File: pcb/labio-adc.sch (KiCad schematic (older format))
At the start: 10 parts

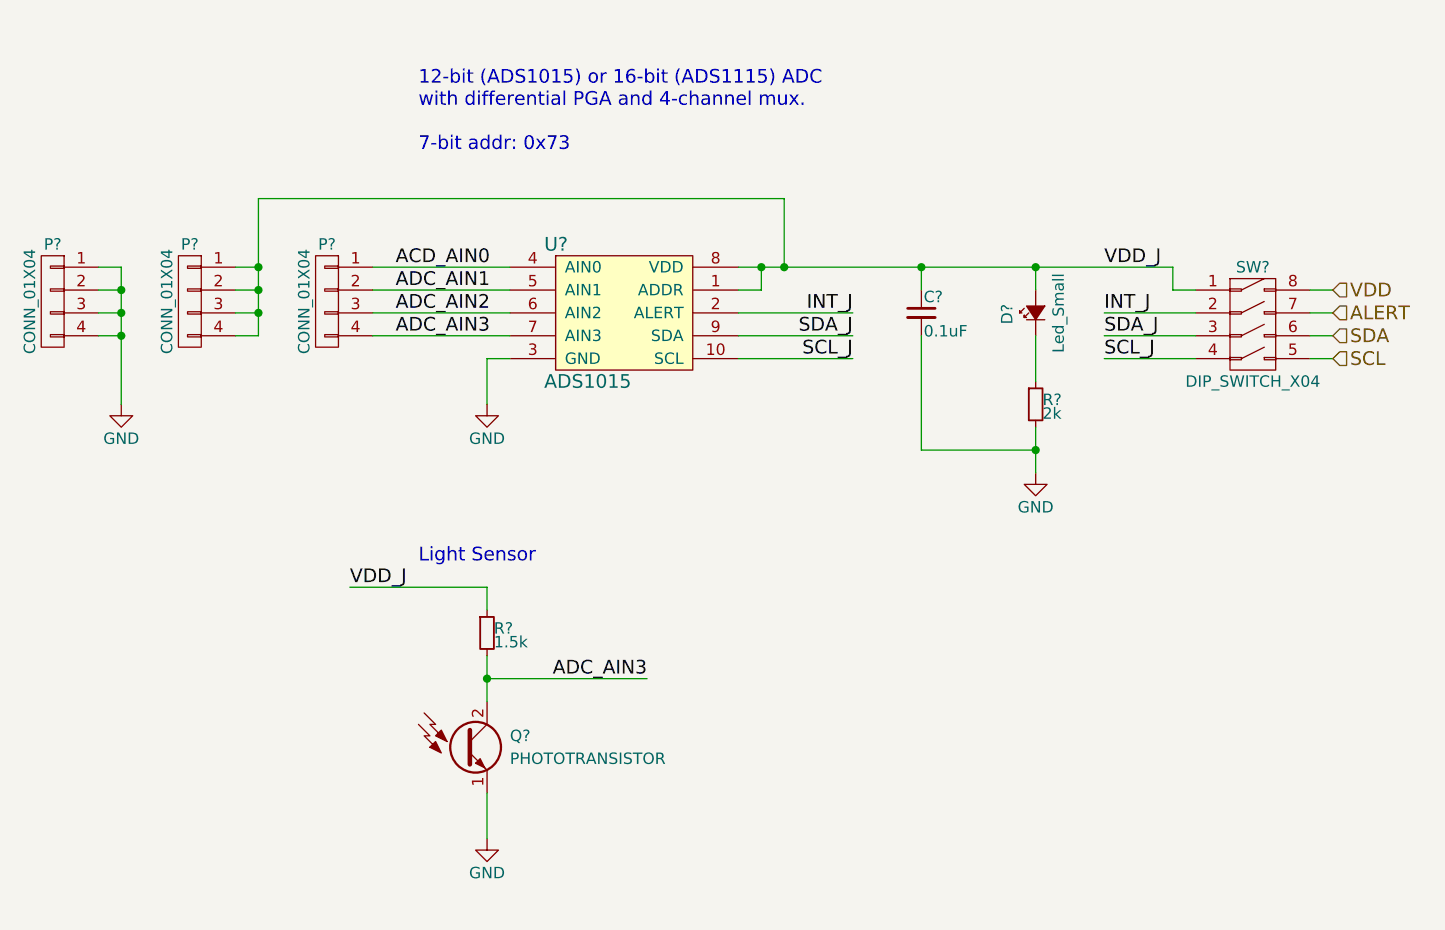
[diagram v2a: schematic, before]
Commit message: make extra footprints. start floorplan. fix display nets. add power expansion header.
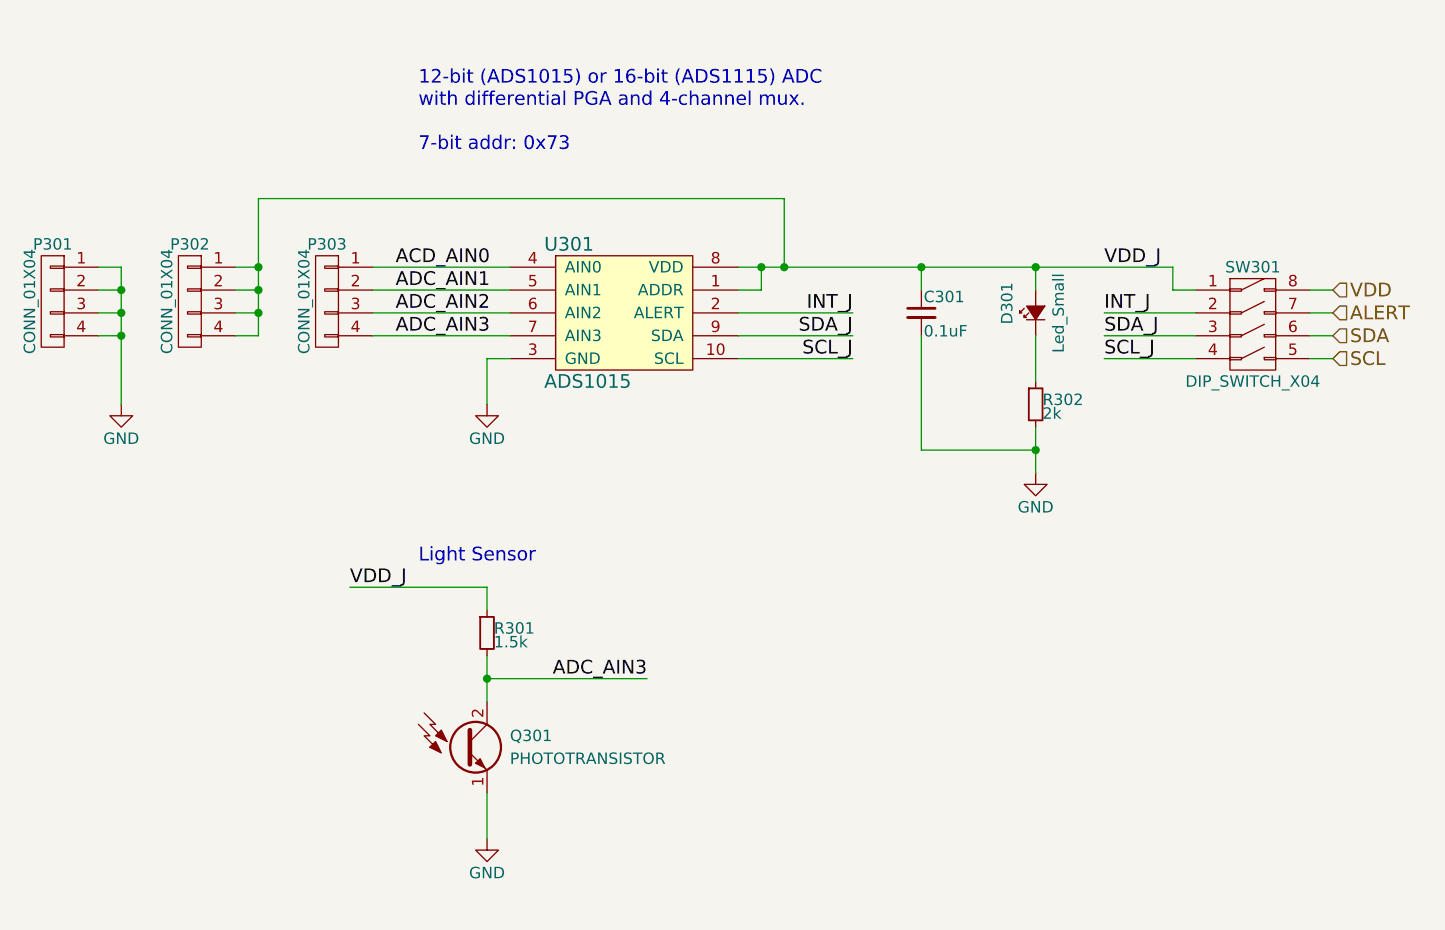
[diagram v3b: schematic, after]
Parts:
- C301: renamed from C?; footprint (none) -> Capacitors_SMD:C_0603
- D301: renamed from D?; footprint (none) -> LEDs:LED-0603
- P301, P302, P303: renamed from P?; footprint (none) -> Pin_Headers:Pin_Header_Straight_1x04
- Q301: renamed from Q?; footprint (none) -> LEDs:LED-0603
- R301, R302: renamed from R?; footprint (none) -> Resistors_SMD:R_0603
- SW301: renamed from SW?; footprint (none) -> labio-special:DIP-8_W7.62mm_SMT
- U301: renamed from U?; footprint (none) -> Housings_SSOP:MSOP-10_3x3mm_Pitch0.5mm
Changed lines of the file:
@@
 $Descr A4 11693 8268
 encoding utf-8
-Sheet 3 8
+Sheet 3 9
 Title ""
 Date ""
@@
 $EndDescr
 $Comp
-L ADS1015 U?
+L ADS1015 U301
 U 1 1 574C563E
 P 6300 3400
-F 0 "U?" H 5950 3700 60  0000 L CNN
+F 0 "U301" H 5950 3700 60  0000 L CNN
 F 1 "ADS1015" H 5950 3100 60  0000 L CNN
-F 2 "" H 6300 3400 60  0000 C CNN
+F 2 "Housings_SSOP:MSOP-10_3x3mm_Pitch0.5mm" H 6300 3400 60  0001 C CNN
 F 3 "" H 6300 3400 60  0000 C CNN
 	1    6300 3400
@@
 $EndComp
 $Comp
-L CONN_01X04 P?
+L CONN_01X04 P301
 U 1 1 574C66B3
 P 3800 3350
-F 0 "P?" H 3800 3600 50  0000 C CNN
+F 0 "P301" H 3800 3600 50  0000 C CNN
 F 1 "CONN_01X04" V 3900 3350 50  0000 C CNN
-F 2 "" H 3800 3350 50  0000 C CNN
+F 2 "Pin_Headers:Pin_Header_Straight_1x04" H 3800 3350 50  0001 C CNN
 F 3 "" H 3800 3350 50  0000 C CNN
 	1    3800 3350
@@
 $EndComp
 $Comp
-L CONN_01X04 P?
+L CONN_01X04 P302
 U 1 1 574C66E4
 P 4400 3350
-F 0 "P?" H 4400 3600 50  0000 C CNN
+F 0 "P302" H 4400 3600 50  0000 C CNN
 F 1 "CONN_01X04" V 4500 3350 50  0000 C CNN
-F 2 "" H 4400 3350 50  0000 C CNN
+F 2 "Pin_Headers:Pin_Header_Straight_1x04" H 4400 3350 50  0001 C CNN
 F 3 "" H 4400 3350 50  0000 C CNN
 	1    4400 3350
@@
 $EndComp
 $Comp
-L CONN_01X04 P?
+L CONN_01X04 P303
 U 1 1 574C66FC
 P 5000 3350
-F 0 "P?" H 5000 3600 50  0000 C CNN
+F 0 "P303" H 5000 3600 50  0000 C CNN
 F 1 "CONN_01X04" V 5100 3350 50  0000 C CNN
-F 2 "" H 5000 3350 50  0000 C CNN
+F 2 "Pin_Headers:Pin_Header_Straight_1x04" H 5000 3350 50  0001 C CNN
 F 3 "" H 5000 3350 50  0000 C CNN
 	1    5000 3350
@@
 $EndComp
 $Comp
-L GND #PWR?
+L GND #PWR05
 U 1 1 574C6823
 P 5700 3800
-F 0 "#PWR?" H 5700 3550 50  0001 C CNN
+F 0 "#PWR05" H 5700 3550 50  0001 C CNN
 F 1 "GND" H 5700 3650 50  0000 C CNN
 F 2 "" H 5700 3800 50  0000 C CNN
@@
 $EndComp
 $Comp
-L C_Small C?
+L C_Small C301
 U 1 1 574C68FF
 P 7600 3400
-F 0 "C?" H 7610 3470 50  0000 L CNN
+F 0 "C301" H 7610 3470 50  0000 L CNN
 F 1 "0.1uF" H 7610 3320 50  0000 L CNN
-F 2 "" H 7600 3400 50  0000 C CNN
+F 2 "Capacitors_SMD:C_0603" H 7600 3400 50  0001 C CNN
 F 3 "" H 7600 3400 50  0000 C CNN
 	1    7600 3400
@@
 	5700 3600 5800 3600
 Wire Wire Line
-	4100 3200 4100 3300
-Wire Wire Line
-	4100 3300 4100 3400
-Wire Wire Line
-	4100 3400 4100 3500
-Wire Wire Line
-	4100 3500 4100 3800
+	4100 3200 4100 3800
 Wire Wire Line
 	4100 3200 4000 3200
@@
 	4700 3500 4600 3500
 Wire Wire Line
-	4700 2900 4700 3200
-Wire Wire Line
-	4700 3200 4700 3300
-Wire Wire Line
-	4700 3300 4700 3400
-Wire Wire Line
-	4700 3400 4700 3500
+	4700 2900 4700 3500
 Wire Wire Line
 	4700 2900 7000 2900
@@
 	5200 3500 5800 3500
 $Comp
-L PHOTOTRANSISTOR Q?
+L PHOTOTRANSISTOR Q301
 U 1 1 576D542D
 P 5600 5300
-F 0 "Q?" H 5800 5350 50  0000 L CNN
+F 0 "Q301" H 5800 5350 50  0000 L CNN
 F 1 "PHOTOTRANSISTOR" H 5800 5250 50  0000 L CNN
-F 2 "" H 5800 5400 50  0000 C CNN
+F 2 "LEDs:LED-0603" H 5800 5400 50  0001 C CNN
 F 3 "" H 5600 5300 50  0000 C CNN
 	1    5600 5300
@@
 $EndComp
 $Comp
-L GND #PWR?
+L GND #PWR06
 U 1 1 576D549A
 P 5700 5700
-F 0 "#PWR?" H 5700 5450 50  0001 C CNN
+F 0 "#PWR06" H 5700 5450 50  0001 C CNN
 F 1 "GND" H 5700 5550 50  0000 C CNN
 F 2 "" H 5700 5700 50  0000 C CNN
@@
 $EndComp
 $Comp
-L R_Small R?
+L R_Small R301
 U 1 1 576D54B9
 P 5700 4800
-F 0 "R?" H 5730 4820 50  0000 L CNN
+F 0 "R301" H 5730 4820 50  0000 L CNN
 F 1 "1.5k" H 5730 4760 50  0000 L CNN
-F 2 "" H 5700 4800 50  0000 C CNN
+F 2 "Resistors_SMD:R_0603" H 5700 4800 50  0001 C CNN
 F 3 "" H 5700 4800 50  0000 C CNN
 	1    5700 4800
@@
 	5700 4600 5100 4600
 Wire Wire Line
-	5700 4900 5700 5000
-Wire Wire Line
-	5700 5000 5700 5100
+	5700 4900 5700 5100
 Wire Wire Line
 	5700 5000 6400 5000
@@
 ADC_AIN3
 $Comp
-L DIP_SWITCH_X04 SW?
+L DIP_SWITCH_X04 SW301
 U 1 1 576D562D
 P 9050 3450
-F 0 "SW?" H 9050 3700 50  0000 C CNN
+F 0 "SW301" H 9050 3700 50  0000 C CNN
 F 1 "DIP_SWITCH_X04" H 9050 3200 50  0000 C CNN
-F 2 "" H 9050 2250 50  0000 C CNN
+F 2 "labio-special:DIP-8_W7.62mm_SMT" H 9050 2250 50  0001 C CNN
 F 3 "" H 9050 2250 50  0000 C CNN
 	1    9050 3450
@@
 $EndComp
 $Comp
-L Led_Small D?
+L Led_Small D301
 U 1 1 576D57C2
 P 8100 3400
-F 0 "D?" H 8050 3525 50  0000 L CNN
+F 0 "D301" H 8050 3525 50  0000 L CNN
 F 1 "Led_Small" H 7925 3300 50  0000 L CNN
-F 2 "" V 8100 3400 50  0000 C CNN
+F 2 "LEDs:LED-0603" V 8100 3400 50  0001 C CNN
 F 3 "" V 8100 3400 50  0000 C CNN
 	1    8100 3400
@@
 $EndComp
 $Comp
-L R_Small R?
+L R_Small R302
 U 1 1 576D5877
 P 8100 3800
-F 0 "R?" H 8130 3820 50  0000 L CNN
+F 0 "R302" H 8130 3820 50  0000 L CNN
 F 1 "2k" H 8130 3760 50  0000 L CNN
-F 2 "" H 8100 3800 50  0000 C CNN
+F 2 "Resistors_SMD:R_0603" H 8100 3800 50  0001 C CNN
 F 3 "" H 8100 3800 50  0000 C CNN
 	1    8100 3800
@@
 	5700 3800 5700 3600
 $Comp
-L GND #PWR?
+L GND #PWR07
 U 1 1 576D595B
 P 4100 3800
-F 0 "#PWR?" H 4100 3550 50  0001 C CNN
+F 0 "#PWR07" H 4100 3550 50  0001 C CNN
 F 1 "GND" H 4100 3650 50  0000 C CNN
 F 2 "" H 4100 3800 50  0000 C CNN
@@
 $EndComp
 $Comp
-L GND #PWR?
+L GND #PWR08
 U 1 1 576D5995
 P 8100 4100
-F 0 "#PWR?" H 8100 3850 50  0001 C CNN
+F 0 "#PWR08" H 8100 3850 50  0001 C CNN
 F 1 "GND" H 8100 3950 50  0000 C CNN
 F 2 "" H 8100 4100 50  0000 C CNN
@@
 $EndComp
 Wire Wire Line
-	8100 3900 8100 4000
-Wire Wire Line
-	8100 4000 8100 4100
+	8100 3900 8100 4100
 Wire Wire Line
 	8100 4000 7600 4000
@@
 	8700 3300 8700 3200
 Wire Wire Line
-	8700 3200 8100 3200
-Wire Wire Line
-	8100 3200 7600 3200
-Wire Wire Line
-	7600 3200 7000 3200
-Wire Wire Line
-	7000 3200 6900 3200
-Wire Wire Line
-	6900 3200 6800 3200
+	8700 3200 6800 3200
 Wire Wire Line
 	6900 3300 6900 3200

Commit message: update imu parts, adc rails, motor headers
* replace LSM303C accelerometer with LSM303D for better sensor ranges at same cost.
* add L3GD20H gyroscope so we have a 10-DOF imu. consider leaving depopulated for complexity.
* add 0 ohms to accel/gyro address and interrupt pins in case of later changes
* change ADC rails to 5V to read 5V power shunts. add level shifters to the 3.3V I2C bus.
* use 3.5mm pitch headers for motor terminal blocks to accept higher guage wire.

todo:
* redo ADC routing
* make space behind motor headers
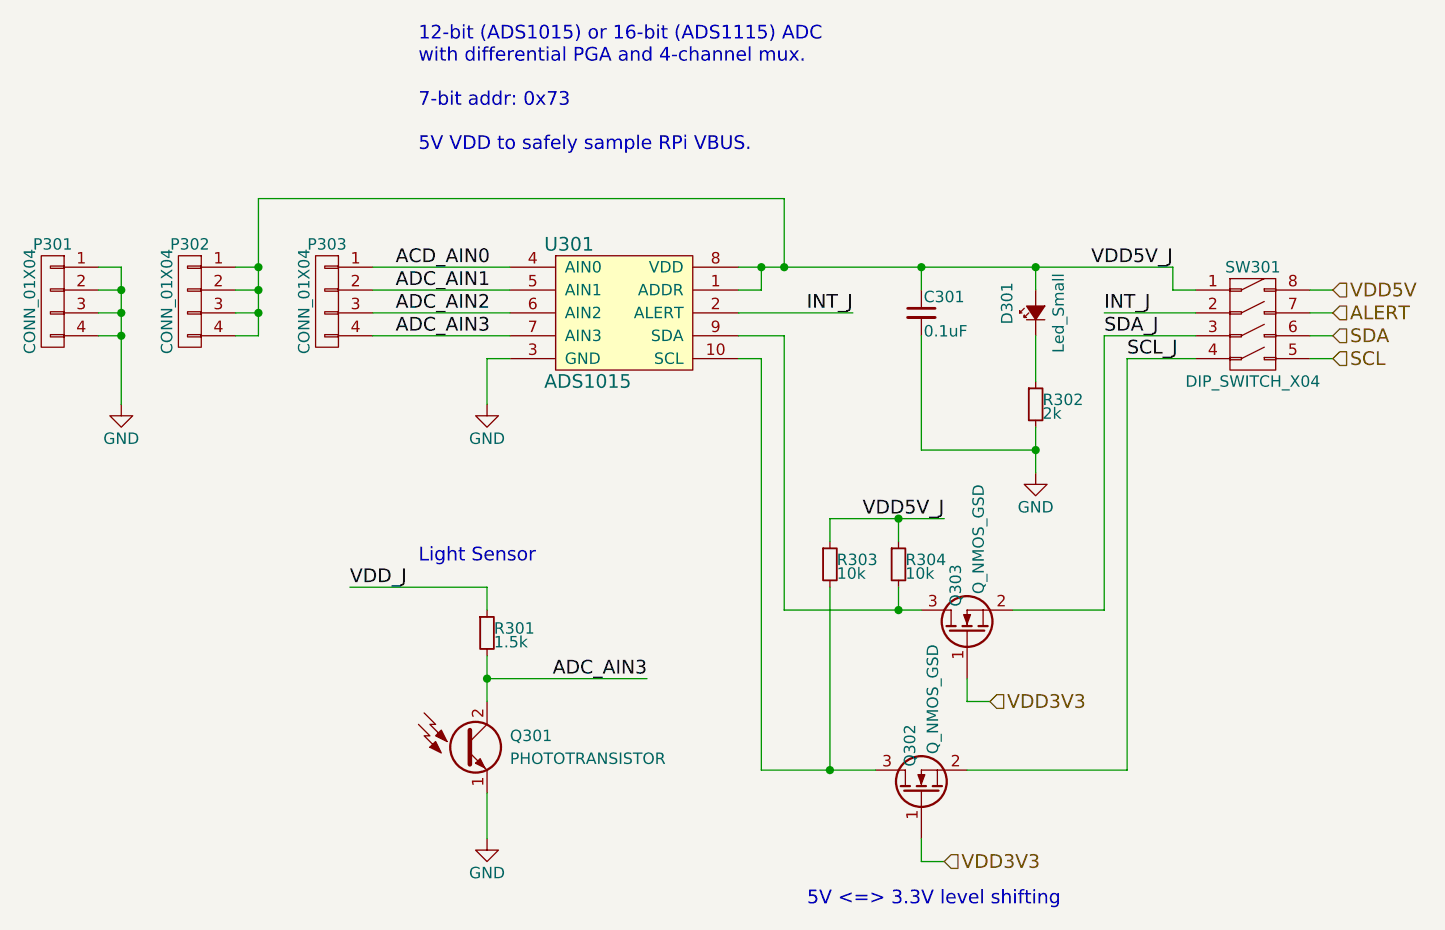
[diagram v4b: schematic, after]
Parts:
- added Q302, Q303: Q_NMOS_GSD, TO_SOT_Packages_SMD:SOT-23, symbol Q_NMOS_GSD
- added R303, R304: 10k, Resistors_SMD:R_0603, symbol R_Small
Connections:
- net SCL_J: now also Q302.2 (S); no longer U301.10 (SCL)
- net SDA_J: now also Q303.2 (S); no longer U301.9 (SDA)
- net VDD_J: no longer C301.1, D301.2 (A), P302.1 (P1), P302.2 (P2), P302.3 (P3), P302.4 (P4), SW301.1 (1A), U301.1 (ADDR), U301.8 (VDD)
- net VDD renamed VDD5V
- new net: Q302.3 (D), R303.2, U301.10 (SCL)
- new net: Q303.3 (D), R304.2, U301.9 (SDA)
- new net VDD3V3: Q302.1 (G), Q303.1 (G)
- new net VDD5V_J: C301.1, D301.2 (A), P302.1 (P1), P302.2 (P2), P302.3 (P3), P302.4 (P4), R303.1, R304.1, SW301.1 (1A), U301.1 (ADDR), U301.8 (VDD)
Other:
- note added: "12-bit (ADS1015) or 16-bit (ADS1115) ADC\nwith differential PGA and 4-channel mux.\n\n7-bit addr: 0x73\n\n5V VDD to safely sample RPi VBUS."
- note added: "5V <=> 3.3V level shifting"
- note removed: "12-bit (ADS1015) or 16-bit (ADS1115) ADC\nwith differential PGA and 4-channel mux.\n\n7-bit addr: 0x73"
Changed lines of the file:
@@
 $EndComp
 Text HLabel 9400 3300 2    60   Input ~ 0
-VDD
+VDD5V
 Text HLabel 9400 3500 2    60   Input ~ 0
 SDA
@@
 	6800 3400 7300 3400
 Wire Wire Line
-	7300 3500 6800 3500
-Wire Wire Line
-	6800 3600 7300 3600
-Wire Wire Line
 	5200 3200 5800 3200
 Wire Wire Line
@@
 	6800 3300 6900 3300
 Text Notes 5400 2700 0    60   ~ 0
-12-bit (ADS1015) or 16-bit (ADS1115) ADC\nwith differential PGA and 4-channel mux.\n\n7-bit addr: 0x73
+12-bit (ADS1015) or 16-bit (ADS1115) ADC\nwith differential PGA and 4-channel mux.\n\n7-bit addr: 0x73\n\n5V VDD to safely sample RPi VBUS.
 Text Label 5300 3200 0    60   ~ 0
 ACD_AIN0
@@
 	8400 3500 8800 3500
 Wire Wire Line
-	8800 3600 8400 3600
+	8800 3600 8500 3600
 Wire Wire Line
 	8800 3300 8700 3300
@@
 Wire Wire Line
 	9300 3600 9400 3600
-Text Label 8400 3200 0    60   ~ 0
-VDD_J
+Text Label 8700 3200 2    60   ~ 0
+VDD5V_J
 Text Label 8400 3400 0    60   ~ 0
 INT_J
 Text Label 8400 3500 0    60   ~ 0
 SDA_J
-Text Label 8400 3600 0    60   ~ 0
+Text Label 8500 3600 0    60   ~ 0
 SCL_J
 Text Label 7300 3400 2    60   ~ 0
 INT_J
-Text Label 7300 3500 2    60   ~ 0
-SDA_J
-Text Label 7300 3600 2    60   ~ 0
-SCL_J
 Text Label 5100 4600 0    60   ~ 0
 VDD_J
+$Comp
+L Q_NMOS_GSD Q303
+U 1 1 578AEC2F
+P 7800 4800
+F 0 "Q303" H 8100 4850 50  0000 R CNN
+F 1 "Q_NMOS_GSD" H 8450 4750 50  0000 R CNN
+F 2 "TO_SOT_Packages_SMD:SOT-23" H 8000 4900 50  0001 C CNN
+F 3 "" H 7800 4800 50  0000 C CNN
+	1    7800 4800
+	0    -1   -1   0
+$EndComp
+$Comp
+L Q_NMOS_GSD Q302
+U 1 1 578AECE5
+P 7600 5500
+F 0 "Q302" H 7900 5550 50  0000 R CNN
+F 1 "Q_NMOS_GSD" H 8250 5450 50  0000 R CNN
+F 2 "TO_SOT_Packages_SMD:SOT-23" H 7800 5600 50  0001 C CNN
+F 3 "" H 7600 5500 50  0000 C CNN
+	1    7600 5500
+	0    -1   -1   0
+$EndComp
+$Comp
+L R_Small R304
+U 1 1 578AED3B
+P 7500 4500
+F 0 "R304" H 7530 4520 50  0000 L CNN
+F 1 "10k" H 7530 4460 50  0000 L CNN
+F 2 "Resistors_SMD:R_0603" H 7500 4500 50  0001 C CNN
+F 3 "" H 7500 4500 50  0000 C CNN
+	1    7500 4500
+	1    0    0    -1
+$EndComp
+$Comp
+L R_Small R303
+U 1 1 578AED89
+P 7200 4500
+F 0 "R303" H 7230 4520 50  0000 L CNN
+F 1 "10k" H 7230 4460 50  0000 L CNN
+F 2 "Resistors_SMD:R_0603" H 7200 4500 50  0001 C CNN
+F 3 "" H 7200 4500 50  0000 C CNN
+	1    7200 4500
+	1    0    0    -1
+$EndComp
+Wire Wire Line
+	7800 5000 7800 5100
+Wire Wire Line
+	7800 5100 7900 5100
+Wire Wire Line
+	7600 5700 7600 5800
+Wire Wire Line
+	7600 5800 7700 5800
+Text HLabel 7900 5100 2    60   Input ~ 0
+VDD3V3
+Text HLabel 7700 5800 2    60   Input ~ 0
+VDD3V3
+Wire Wire Line
+	6800 3600 6900 3600
+Wire Wire Line
+	6900 3600 6900 5400
+Wire Wire Line
+	6900 5400 7400 5400
+Wire Wire Line
+	6800 3500 7000 3500
+Wire Wire Line
+	7000 3500 7000 4700
+Wire Wire Line
+	7000 4700 7600 4700
+Wire Wire Line
+	7200 4600 7200 5400
+Connection ~ 7200 5400
+Wire Wire Line
+	7500 4600 7500 4700
+Connection ~ 7500 4700
+Wire Wire Line
+	7200 4400 7200 4300
+Wire Wire Line
+	7200 4300 7700 4300
+Wire Wire Line
+	7500 4400 7500 4300
+Connection ~ 7500 4300
+Text Label 7700 4300 2    60   ~ 0
+VDD5V_J
+Wire Wire Line
+	8400 3500 8400 4700
+Wire Wire Line
+	8400 4700 8000 4700
+Wire Wire Line
+	7800 5400 8500 5400
+Wire Wire Line
+	8500 5400 8500 3600
+Text Notes 7100 6000 0    60   ~ 0
+5V <=> 3.3V level shifting
 $EndSCHEMATC
